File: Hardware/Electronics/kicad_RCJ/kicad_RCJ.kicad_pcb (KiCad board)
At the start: 2 copper layers, 52 parts, among them J10 Conn_01x04_M1_extra, J11 Conn_01x04_M2_extra, J12 Conn_01x04_M3_extra, J13 Conn_01x04_M4_extra, J14 Conn_01x06_teensy_left_extra, J15 Conn_01x04_teensy_right_extra, J16 Conn_01x07_IO_expander_extra, J17 Conn_02x03_I2C, J18 Conn_02x05_3V3_GND, J19 Conn_02x05_5V_GND, J2 Conn_01x06_IMU_extra, J20 Conn_01x06_BNO085_extra, J21 Conn_01x06_ISM20948_extra, J22 Conn_01x02_LSM5DSOX_LIS3MDL_e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, J3 Conn_01x02_colsens_interrupt, J4 Conn_01x02_5V, J5 Conn_01x02_3V3, J6 Conn_01x02_I2C1, J7 Conn_01x01_LOP, J8 Conn_01x03_IO_expander_interr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, J9 Conn_01x06_LED, M5 Servo1, M6 Servo2, U12 VL53L0/1X, U13 VL53L0/1X, U14 VL53L0/1X, U15 VL53L0/1X, U16 VL53L0/1X, U17 VL53L0/1X, U18 VL53L0/1X, U23 TCS34725, U24 APDS9960, U25 VL53L0/1X

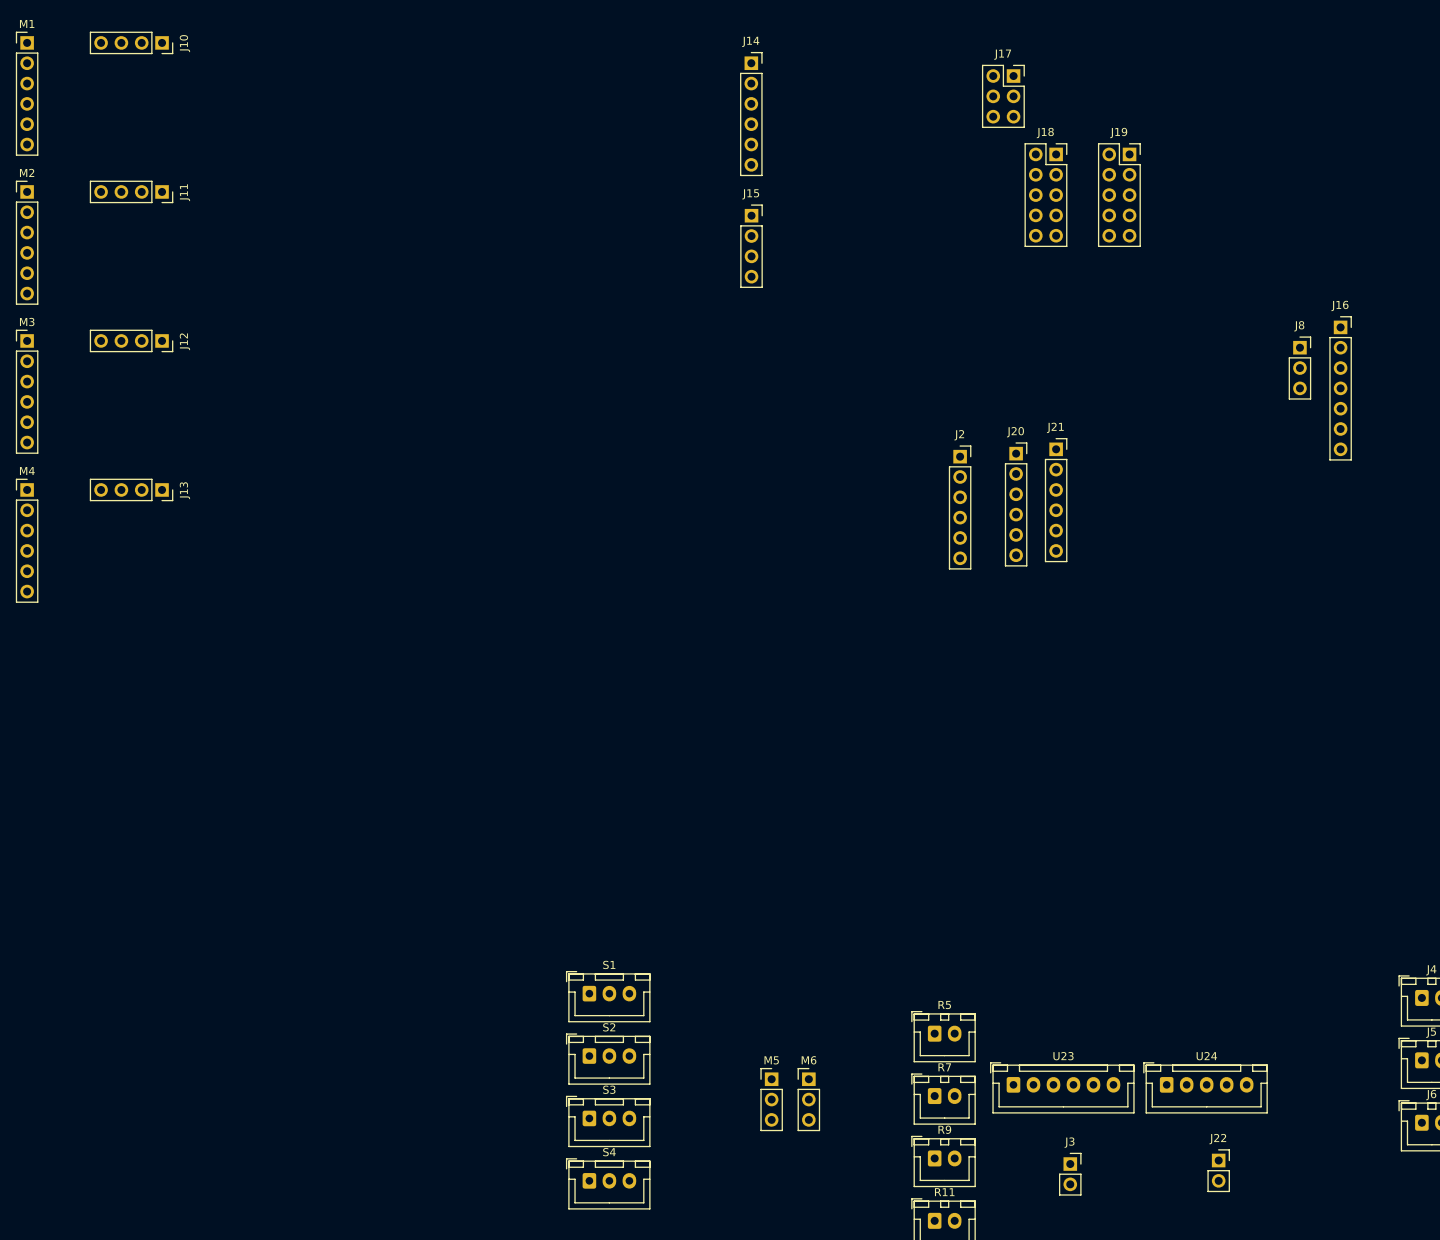
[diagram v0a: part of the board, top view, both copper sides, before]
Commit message: added some footprints and did some PCB layout work
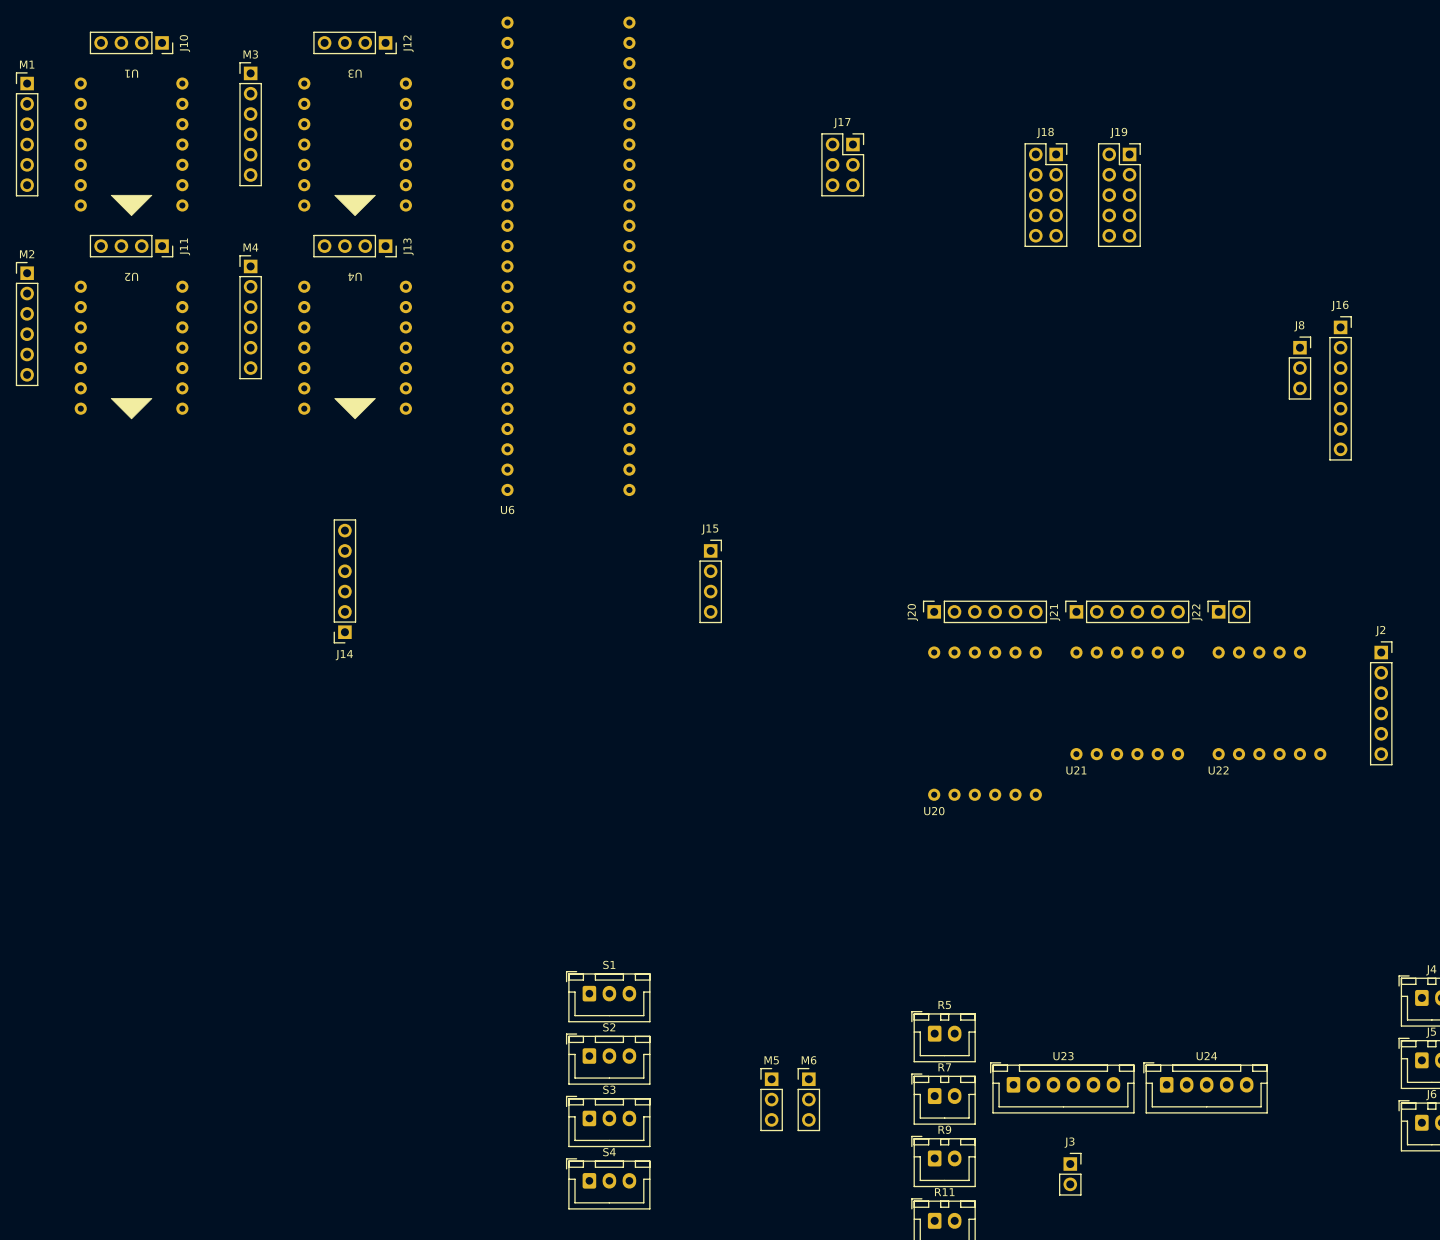
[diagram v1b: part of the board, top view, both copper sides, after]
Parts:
- added U1: DRV8874, RCJ2024_kicad_footprints:DRV8874, F.Cu at (38.1, 22.9)
- added U2: DRV8874, RCJ2024_kicad_footprints:DRV8874, F.Cu at (38.1, 48.3)
- added U20: BNO085, RCJ2024_kicad_footprints:BNO085, F.Cu at (132.1, 111.8)
- added U21: ICM20948, RCJ2024_kicad_footprints:ICM2049, F.Cu at (149.9, 106.7)
- added U22: LSM6DSOX+LIS3MDL, RCJ2024_kicad_footprints:LSM6DSOX+LIS3MDL, F.Cu at (167.6, 106.7)
- added U3: DRV8874, RCJ2024_kicad_footprints:DRV8874, F.Cu at (66.0, 22.9)
- added U4: DRV8874, RCJ2024_kicad_footprints:DRV8874, F.Cu at (66.0, 48.3)
- added U6: ~, RCJ2024_kicad_footprints:Teensy_41, F.Cu at (78.7, 73.7)
- moved J14 87.4 mm to (58.4, 91.4), turned to 180 degrees
- moved J22 68.6 mm to (167.6, 88.9), turned to 90 degrees
- moved J2 58.1 mm to (188.0, 94.0)
- moved J12 46.6 mm to (63.5, 17.8)
- moved M3 43.6 mm to (46.6, 21.6)
- moved J15 42.2 mm to (104.1, 81.3)
- moved J13 41.3 mm to (63.5, 43.2)
- moved M4 39.5 mm to (46.6, 45.7)
- moved J20 22.3 mm to (132.1, 88.9), turned to 90 degrees
- moved J17 21.8 mm to (121.9, 30.5)
- moved J21 20.5 mm to (149.9, 88.9), turned to 90 degrees
- moved M2 10.2 mm to (18.7, 46.6)
- moved J11 6.77 mm to (35.6, 43.2)
- moved M1 5.08 mm to (18.7, 22.9)

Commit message: worked on PCB layout, made footprints etc.
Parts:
- added U19: ~, RCJ2024_kicad_footprints:IO_Expander, F.Cu at (182.9, 55.9)
- moved J17 134.2 mm to (229.6, 110.5)
- moved J18 134.2 mm to (255.0, 111.8)
- moved J19 134.2 mm to (264.2, 111.8)
- moved J14 81.6 mm to (139.7, 99.1), turned to -90 degrees
- moved D7 63.7 mm to (325.6, 128.3)
- moved D4 63.7 mm to (311.8, 128.3)
- moved J4 63.7 mm to (253.9, 156.2)
- moved J5 63.7 mm to (253.9, 164.0)
- moved J6 63.7 mm to (253.9, 171.8)
- moved J7 63.7 mm to (269.1, 169.4)
- moved J9 63.7 mm to (269.1, 174.0)
- moved R11 63.7 mm to (193.0, 184.1)
- moved R5 63.7 mm to (193.0, 160.7)
- moved R7 63.7 mm to (193.0, 168.5)
- moved R9 63.7 mm to (193.0, 176.3)
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
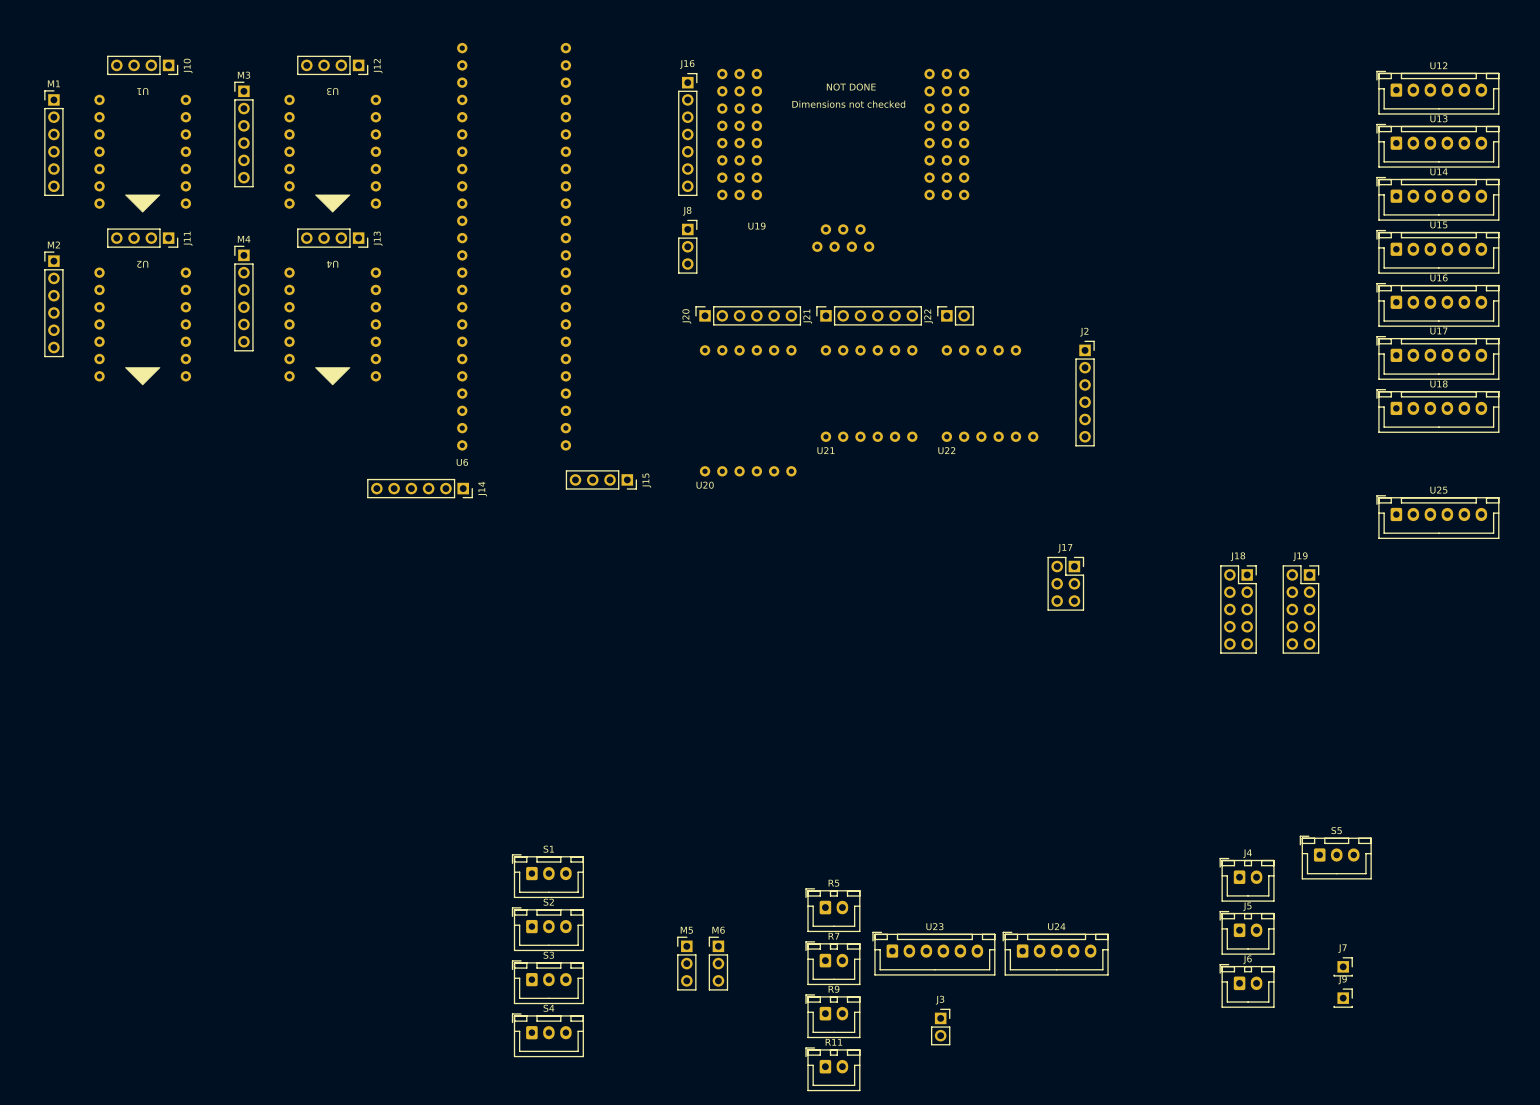
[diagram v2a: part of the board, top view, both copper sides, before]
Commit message: updated PCB layout
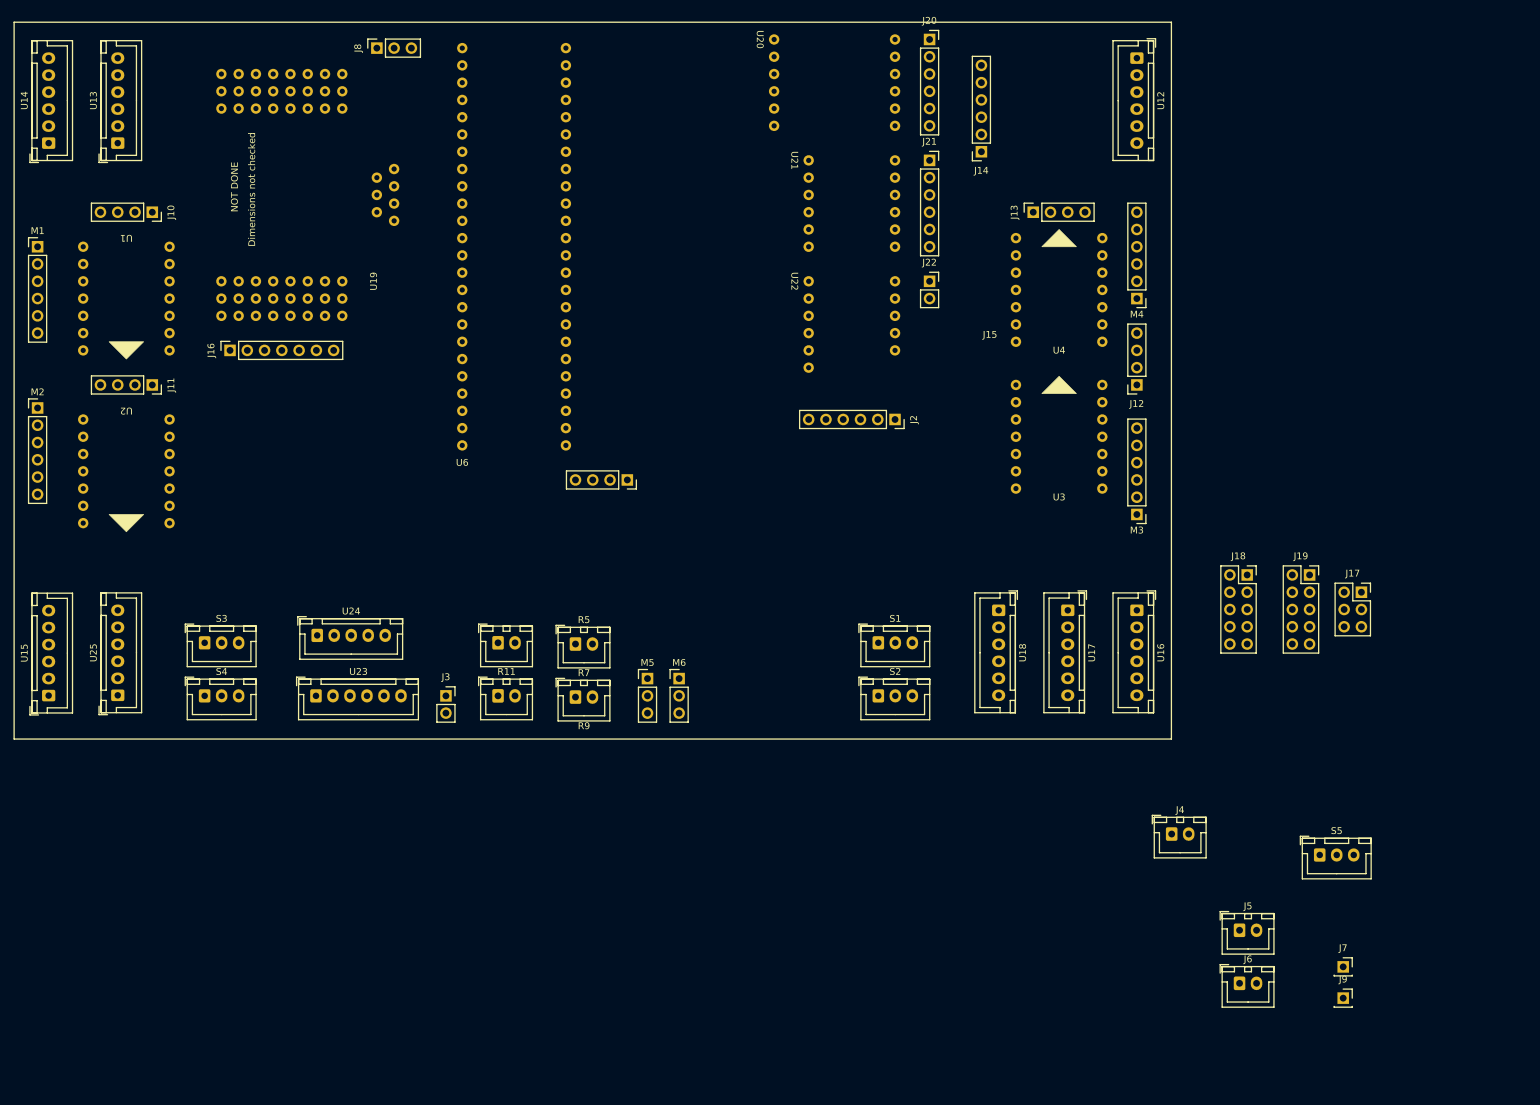
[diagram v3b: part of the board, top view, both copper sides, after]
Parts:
- moved U15 208.8 mm to (78.7, 129.5), turned to 90 degrees
- moved U14 198.3 mm to (78.7, 48.3), turned to 90 degrees
- moved U25 189.9 mm to (88.9, 129.5), turned to 90 degrees
- moved U13 188.0 mm to (88.9, 48.3), turned to 90 degrees
- moved M3 145.3 mm to (238.8, 102.9), turned to 180 degrees
- moved M4 131.5 mm to (238.8, 71.1), turned to 180 degrees
- moved J12 123.7 mm to (238.8, 83.8), turned to 180 degrees
- moved U24 113.6 mm to (118.2, 120.7)
- moved U3 110.1 mm to (221.0, 99.1), turned to 0 degrees
- moved J13 99.3 mm to (223.5, 58.4), turned to 90 degrees
- moved U4 94.7 mm to (221.0, 77.5), turned to 0 degrees
- moved U23 92.7 mm to (118.0, 129.5)
- moved J14 90.9 mm to (215.9, 49.5), turned to 180 degrees
- moved J3 86.8 mm to (137.2, 129.5)
- moved J16 78.0 mm to (105.4, 78.7), turned to 90 degrees
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
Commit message: refined PCB layout and resolved some footprint issues
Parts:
- added R1: R?, Resistor_THT:R_Axial_DIN0207_L6.3mm_D2.5mm_P7.62mm_Horizontal, F.Cu at (166.6, 35.6)
- added R10: R?, Resistor_THT:R_Axial_DIN0207_L6.3mm_D2.5mm_P7.62mm_Horizontal, F.Cu at (149.4, 109.2)
- added R12: R?, Resistor_THT:R_Axial_DIN0207_L6.3mm_D2.5mm_P7.62mm_Horizontal, F.Cu at (144.5, 109.2)
- added R13: R?, Resistor_THT:R_Axial_DIN0207_L6.3mm_D2.5mm_P7.62mm_Horizontal, F.Cu at (43.2, 73.7)
- added R14: R?, Resistor_THT:R_Axial_DIN0207_L6.3mm_D2.5mm_P7.62mm_Horizontal, F.Cu at (50.8, 77.7)
- added R2: R?, Resistor_THT:R_Axial_DIN0207_L6.3mm_D2.5mm_P7.62mm_Horizontal, F.Cu at (162.6, 35.6)
- added R3: R?, Resistor_THT:R_Axial_DIN0207_L6.3mm_D2.5mm_P7.62mm_Horizontal, F.Cu at (171.4, 35.6)
- added R4: R?, Resistor_THT:R_Axial_DIN0207_L6.3mm_D2.5mm_P7.62mm_Horizontal, F.Cu at (175.5, 35.6)
- added R6: R?, Resistor_THT:R_Axial_DIN0207_L6.3mm_D2.5mm_P7.62mm_Horizontal, F.Cu at (160.0, 109.2)
- added R8: R?, Resistor_THT:R_Axial_DIN0207_L6.3mm_D2.5mm_P7.62mm_Horizontal, F.Cu at (154.7, 109.2)
- J9: footprint Connector_PinSocket_2.54mm:PinSocket_1x01_P2.54mm_Vertical -> Connector_PinSocket_2.54mm:PinSocket_1x06_P2.54mm_Vertical
- U12, U13, U14, U15, U16, U17, U18, U25: footprint Connector_JST:JST_XH_B6B-XH-A_1x06_P2.50mm_Vertical -> RCJ2024_kicad_footprints:VL53L0X_VL53L1X_connector
- moved S5 164.5 mm to (106.7, 110.5)
- moved D6 150.0 mm to (172.7, 105.4)
- moved D5 141.7 mm to (176.6, 105.4)
- moved D7 139.1 mm to (188.4, 105.4)
- moved D8 139.1 mm to (193.0, 105.4)
- moved J19 133.8 mm to (130.8, 100.3)
- moved J17 133.6 mm to (138.4, 105.4)
- moved J18 132.3 mm to (123.2, 100.3)
- moved D4 129.7 mm to (184.2, 105.4)
- moved D3 128.9 mm to (180.4, 105.4)
- moved J7 97.8 mm to (182.9, 123.2)
- moved J9 95.1 mm to (193.0, 116.8), turned to -90 degrees
- moved J5 77.1 mm to (189.3, 121.9)
- moved J6 77.1 mm to (189.3, 129.7)
- moved J4 67.9 mm to (179.1, 129.5)
